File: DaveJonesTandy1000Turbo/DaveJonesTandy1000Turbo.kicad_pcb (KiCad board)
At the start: 2 copper layers, 12.7 x 100.3 mm, 12 parts, among them CN1 8284 Socket, J1 TO BUS CLOCK, SW1 ON = TURBO, U1 74LS175, U2 74LS86, U3 8284, Y1 20 / 22 MHz Crystal

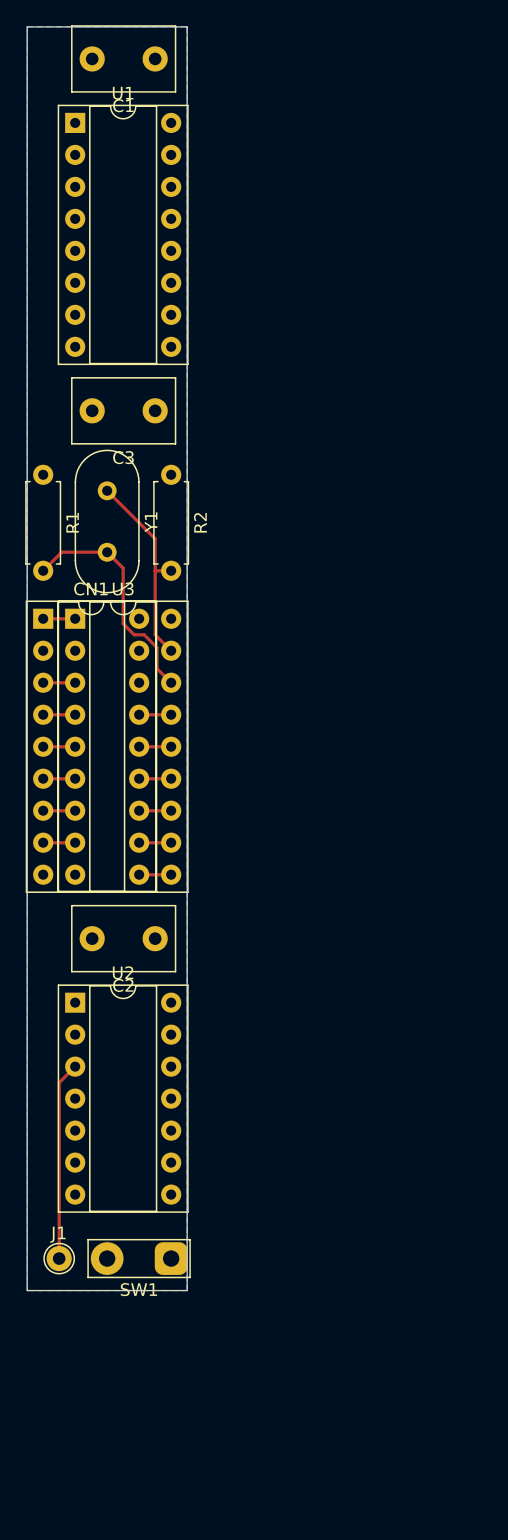
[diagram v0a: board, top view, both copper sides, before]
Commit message: Intial circuit board layout pass done. Still completely untested at this point.
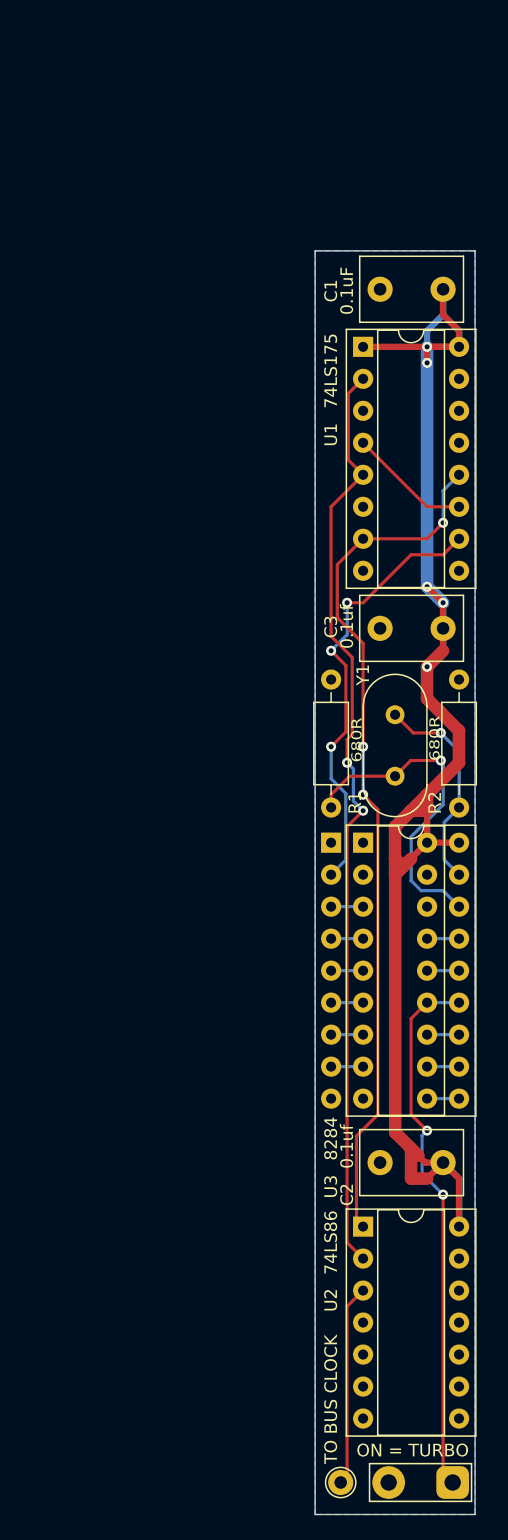
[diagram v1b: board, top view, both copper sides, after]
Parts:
- R1, R2: footprint Resistor_THT:R_Axial_DIN0207_L6.3mm_D2.5mm_P7.62mm_Horizontal -> Resistor_THT:R_Axial_DIN0207_L6.3mm_D2.5mm_P10.16mm_Horizontal
- Y1: value 20 / 22 MHz Crystal -> 20/22MHz Crystal
- moved C1 29.3 mm to (152.4, 53.8)
- moved U2 29.0 mm to (146.1, 128.3)
- moved C2 29.0 mm to (152.4, 123.2)
- moved U1 29.0 mm to (146.1, 58.4)
- moved U3 29.0 mm to (146.1, 97.8)
- moved Y1 29.0 mm to (148.6, 87.6)
- moved CN1 29.0 mm to (143.5, 97.8)
- moved C3 28.7 mm to (152.4, 80.8)
- moved SW1 28.6 mm to (153.2, 148.6)
- moved J1 28.6 mm to (144.3, 148.6)
- moved R1 28.1 mm to (143.5, 84.8)
- moved R2 28.1 mm to (153.7, 84.8)
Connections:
- CN1 pad 1: Net-(CN1-Pad1) -> GND
- CN1 pad 15: Net-(CN1-Pad15) -> GND
- CN1 pad 16: (no net) -> Net-(CN1-Pad16)
- CN1 pad 17: (no net) -> Net-(CN1-Pad17)
- CN1 pad 4: Net-(CN1-Pad4) -> GND
- U1 pad 14: (no net) -> Net-(U1-Pad14)
- U1 pad 15: (no net) -> Net-(U1-Pad15)
- U1 pad 3: (no net) -> Net-(U1-Pad3)
- U1 pad 6: (no net) -> Net-(U1-Pad6)
- U2 pad 11: (no net) -> Net-(U2-Pad11)
- U2 pad 6: (no net) -> Net-(U2-Pad6)
- U2 pad 8: (no net) -> Net-(U2-Pad8)
- U3 pad 1: Net-(CN1-Pad1) -> GND
- U3 pad 15: Net-(CN1-Pad15) -> GND
- U3 pad 2: (no net) -> Net-(U3-Pad2)
- U3 pad 4: Net-(CN1-Pad4) -> GND
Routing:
- net VCC: track 0.00 -> 135.9 mm, vias 0 -> 5
- net Net-(U1-Pad2): track 0.00 -> 74.3 mm, vias 0 -> 2
- net Net-(U1-Pad12): track 0.00 -> 69.0 mm, vias 0 -> 3
- net Net-(CN1-Pad13): track 2.54 -> 44.2 mm, vias 0 -> 2
- net Net-(CN1-Pad2): track 0.00 -> 35.1 mm, vias 0 -> 3
- net Net-(U1-Pad11): track 0.00 -> 9.72 mm
- net Net-(R1-Pad2): track 18.6 -> 26.4 mm, vias 0 -> 1
- net GND: track 0.00 -> 5.08 mm
- net Net-(CN1-Pad4): track 2.54 -> 0.00 mm
- net Net-(CN1-Pad15): track 2.54 -> 0.00 mm
- net Net-(CN1-Pad1): track 2.54 -> 0.00 mm
- net Net-(R2-Pad2): track 16.1 -> 17.3 mm, vias 0 -> 1
- net Net-(J1-Pad1): track 15.8 -> 16.5 mm
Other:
- net class Default: clearance 0.2 -> 0.25
- net class Power added: clearance 0.2, trace_width 0.5, via_dia 0.8, via_drill 0.4
- rule trace_clearance: 0.2 -> 0.25
- board text added: "... and released into the public domain."
- board text added: "Layout by Jayeson Lee-Steere ..."
- board text added: "Original design by Dave Jones"
- board text added: "Published in Electronics Australia April 1991"
